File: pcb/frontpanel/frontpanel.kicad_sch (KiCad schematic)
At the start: 20 parts, among them J1 xx, J2 xx, J3 xx, J4 xx, U1 34.81-7048, U2 MCP9808_MSOP

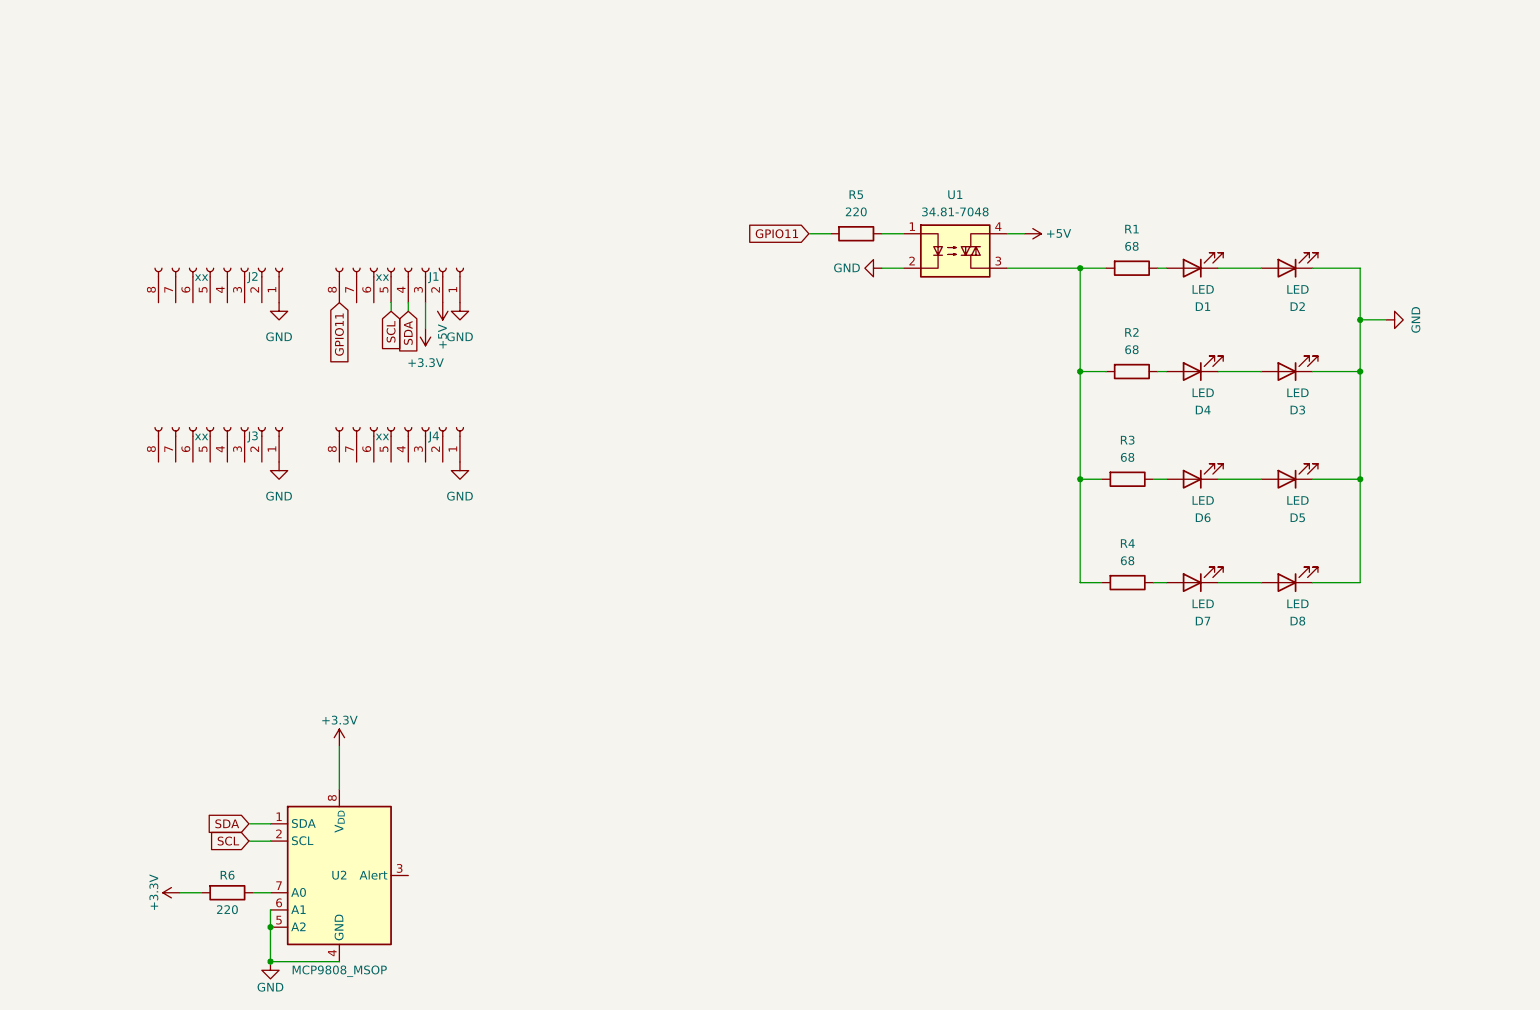
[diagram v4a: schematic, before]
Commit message: [pcb] mono audio, combined sdcard footprint
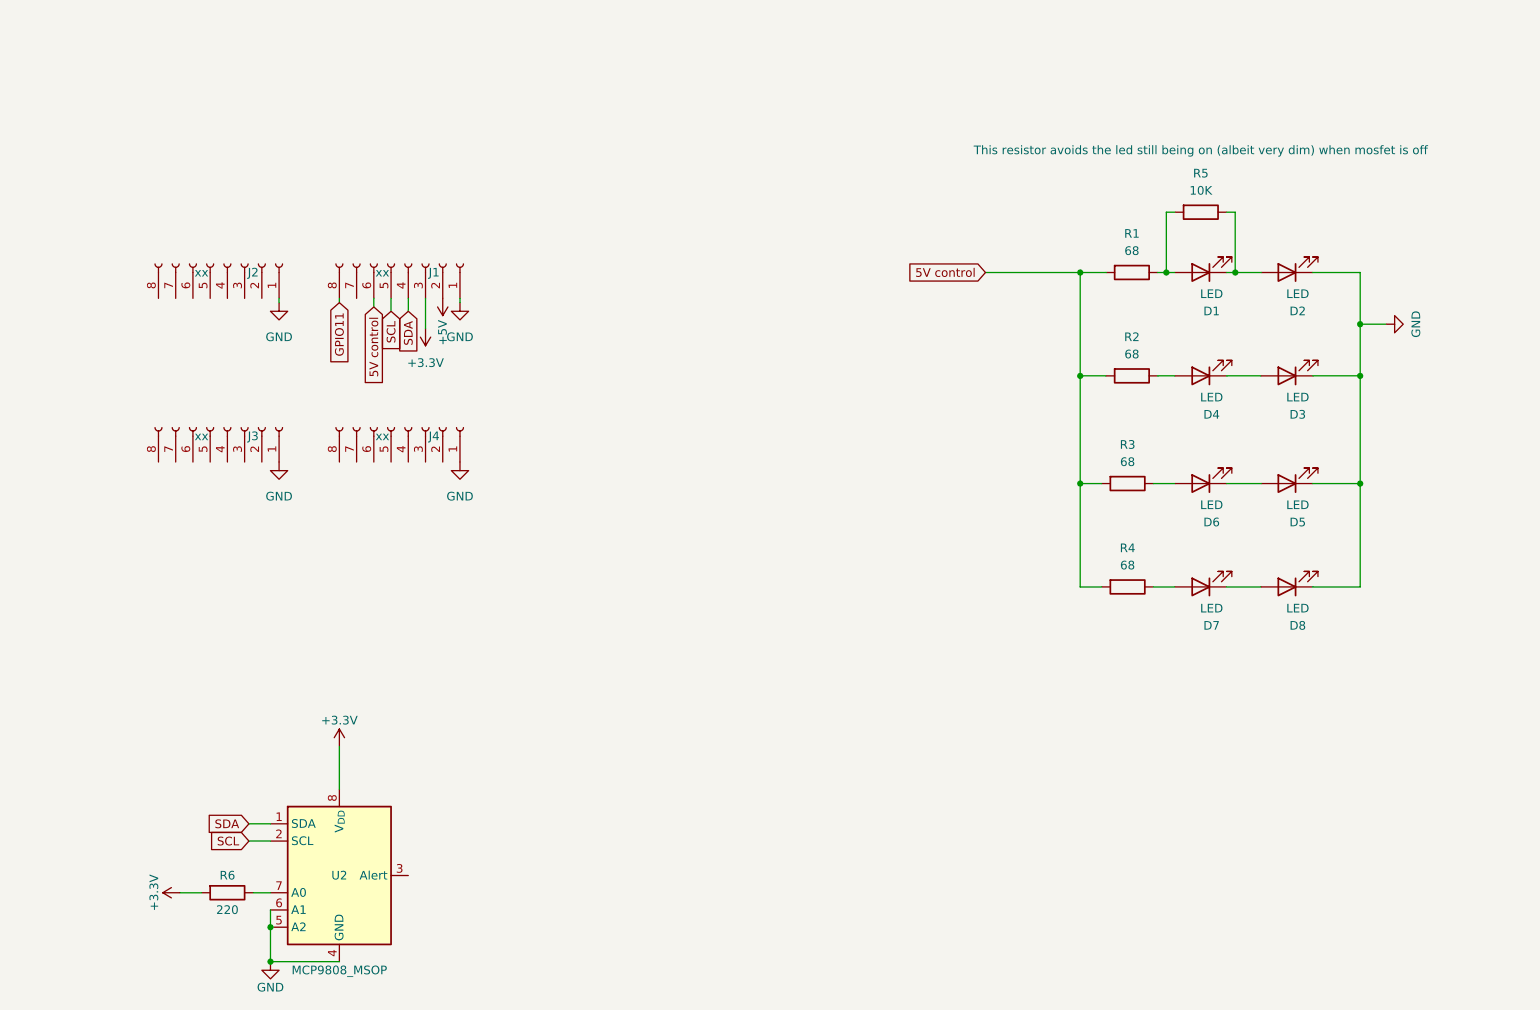
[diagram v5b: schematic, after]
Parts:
- removed U1: 34.81-7048, Package_DIP:SMDIP-4_W7.62mm, symbol Relay_SolidState:FODM3011
- R5: value 220 -> 10K
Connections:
- net GPIO11: no longer R5.2
- net at D1.2 (A), R1.1: now also R5.2
- net 5V control: now reaches R1.2, R2.2, R3.2, R4.2
- net 5V control: now also J1.6 (Pin_6)
- net at D1.1 (K), D2.2 (A): now also R5.1
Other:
- moved on the sheet: D1, D2, D3, D4, D5, D6, D7, D8, J1, J2, R1, R2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
